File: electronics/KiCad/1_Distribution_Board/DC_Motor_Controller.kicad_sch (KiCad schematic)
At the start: 5 parts, among them J8 Conn_01x02, J9 Conn_01x02

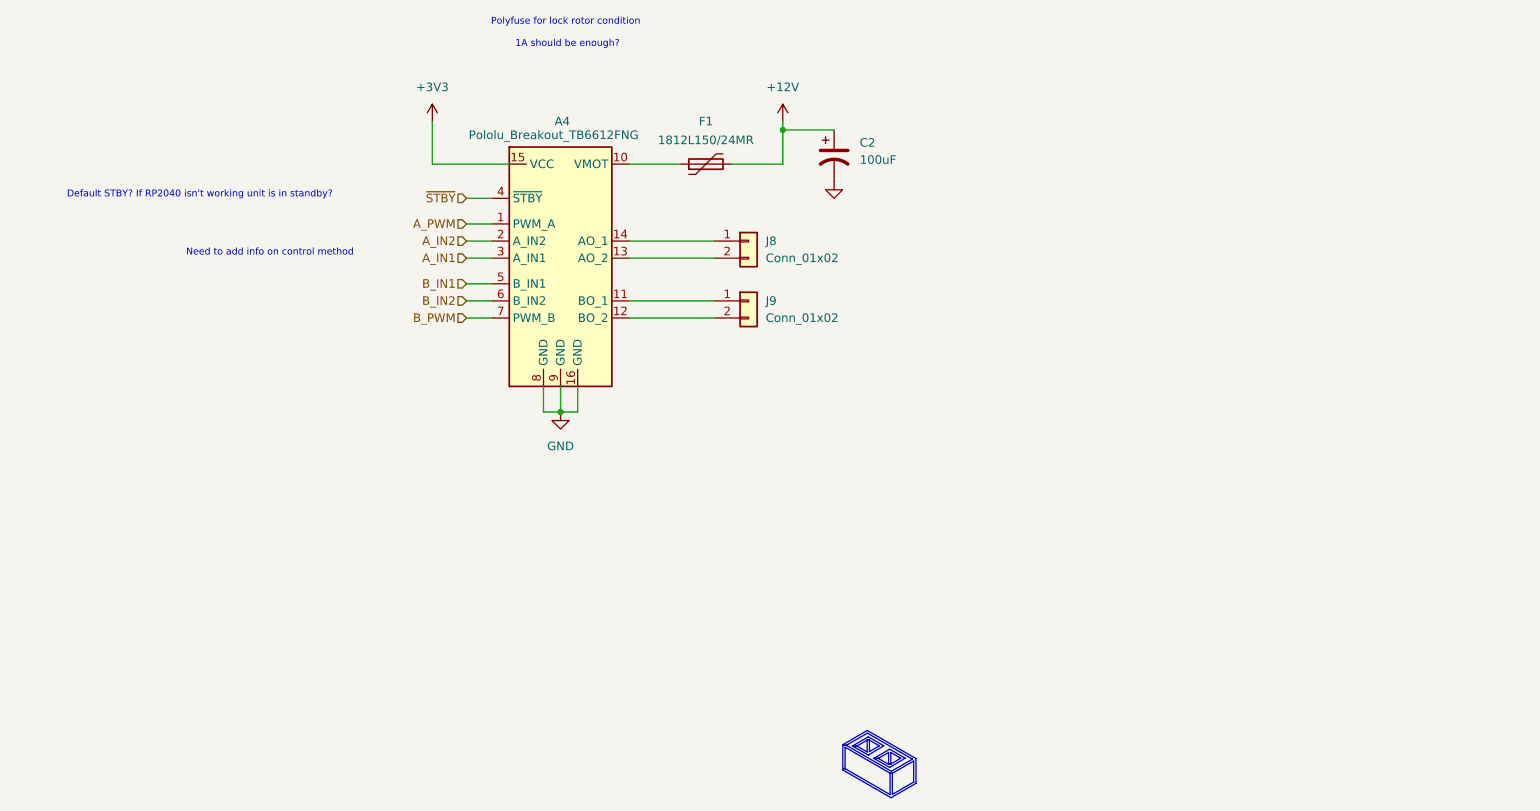
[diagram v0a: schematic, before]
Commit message: Updated Schematic naming, PCB work
Updated Schematic naming for sub-sheets to get rid of untitled and adapter board ones. ADD - 815 sub-sheet for cleaner printable schematic.

PCB:

Started moving modules to socket headers for easy of prototyping.
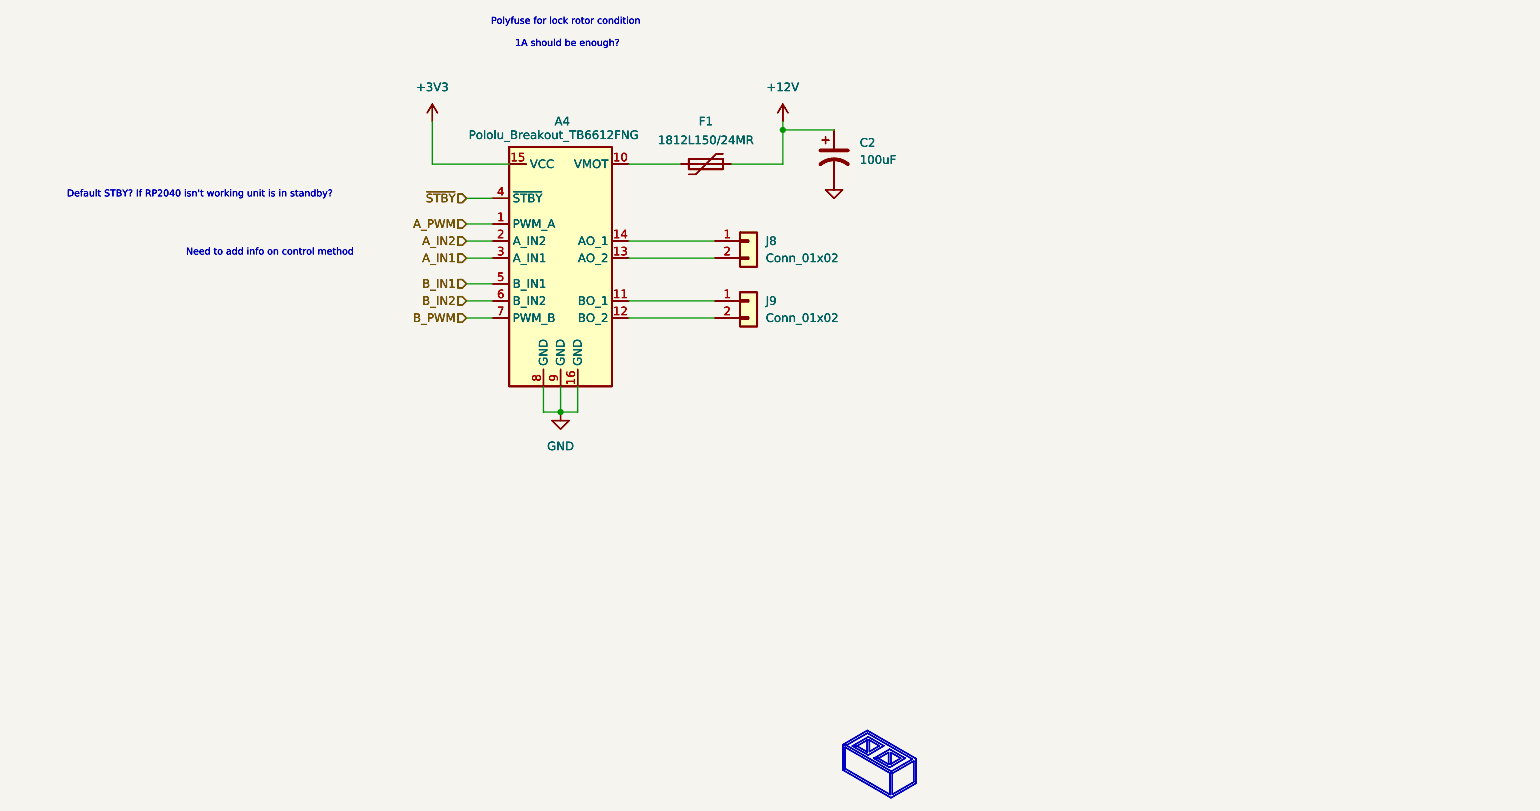
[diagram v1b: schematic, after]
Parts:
- added A4: Pololu_Breakout_TB6612FNG, Module:Pololu_Breakout-16_15.2x20.3mm, symbol JAW:Pololu_Breakout_TB6612FNG
- added C2: 100uF, Capacitor_THT:CP_Radial_D8.0mm_P2.50mm, symbol Device:C_Polarized_US
- added F1: 1812L150/24MR, Fuse:Fuse_1812_4532Metric_Pad1.30x3.40mm_HandSolder, symbol Device:Polyfuse
- added J8, J9: Conn_01x02, Connector_PinHeader_2.54mm:PinHeader_1x02_P2.54mm_Vertical, symbol Connector_Generic:Conn_01x02
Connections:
- net +12V: now also C2.1, F1.2
- net +3V3: now also A4.15 (VCC)
- net A_IN1: now also A4.3 (A_IN1)
- net A_IN2: now also A4.2 (A_IN2)
- net A_PWM: now also A4.1 (PWM_A)
- net B_IN1: now also A4.5 (B_IN1)
- net B_IN2: now also A4.6 (B_IN2)
- net B_PWM: now also A4.7 (PWM_B)
- net GND: now also A4.16 (GND), A4.8 (GND), A4.9 (GND), C2.2
- net ~{STBY}: now also A4.4 (~{STBY})
- net at A4.14 (AO_1), J8.1 (Pin_1): now also A4.14 (AO_1), J8.1 (Pin_1)
- net at A4.13 (AO_2), J8.2 (Pin_2): now also A4.13 (AO_2), J8.2 (Pin_2)
- net at A4.10 (VMOT), F1.1: now also A4.10 (VMOT), F1.1
- net at A4.11 (BO_1), J9.1 (Pin_1): now also A4.11 (BO_1), J9.1 (Pin_1)
- net at A4.12 (BO_2), J9.2 (Pin_2): now also A4.12 (BO_2), J9.2 (Pin_2)

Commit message: PCB updates
Added stepper module headers and working on silk for ease of debug.
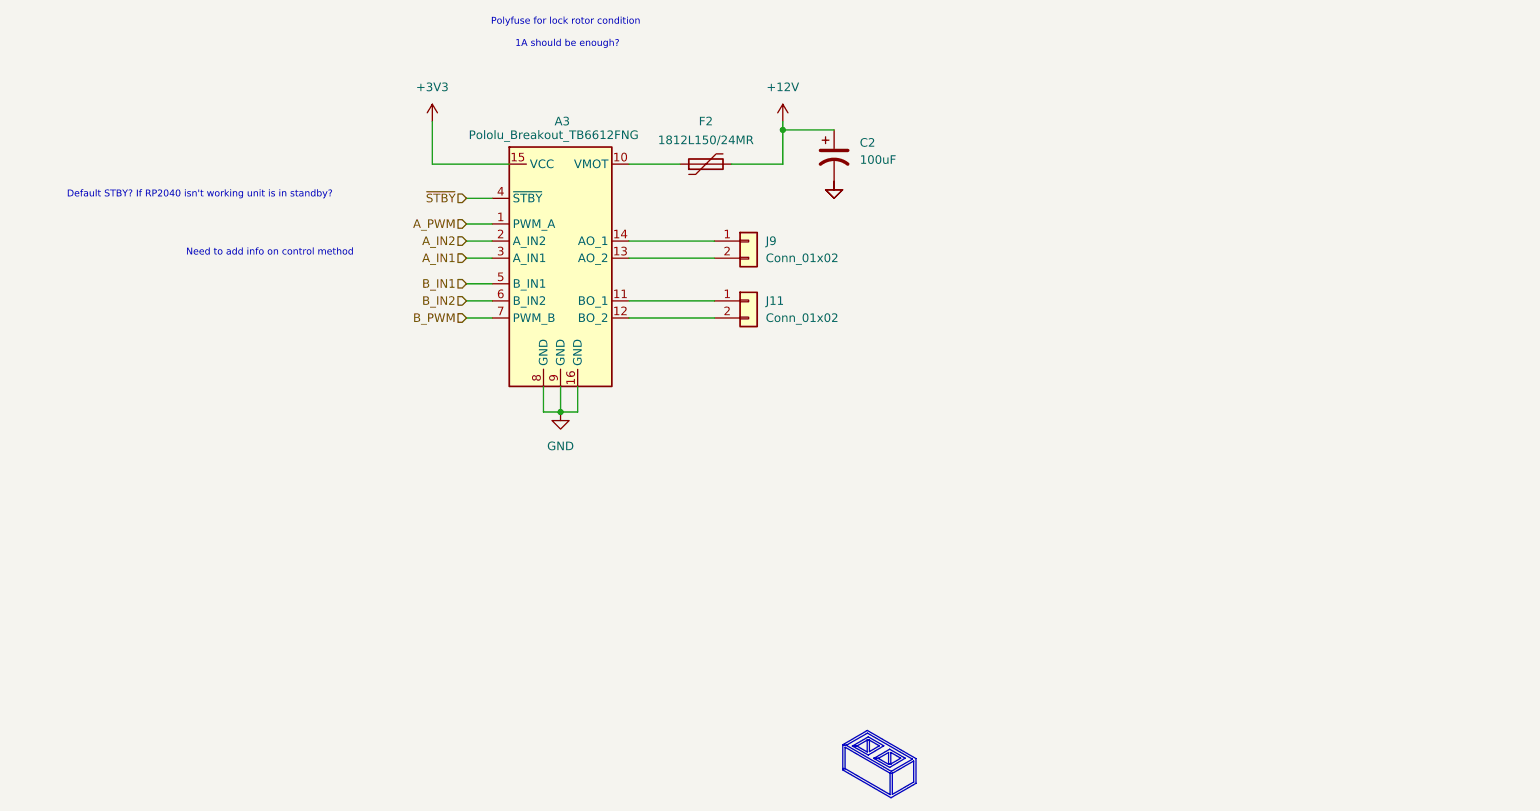
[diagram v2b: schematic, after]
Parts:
- removed A4: Pololu_Breakout_TB6612FNG, Module:Pololu_Breakout-16_15.2x20.3mm, symbol JAW:Pololu_Breakout_TB6612FNG
- removed C2: 100uF, Capacitor_THT:CP_Radial_D8.0mm_P2.50mm, symbol Device:C_Polarized_US
- removed F1: 1812L150/24MR, Fuse:Fuse_1812_4532Metric_Pad1.30x3.40mm_HandSolder, symbol Device:Polyfuse
- removed J8, J9: Conn_01x02, Connector_PinHeader_2.54mm:PinHeader_1x02_P2.54mm_Vertical, symbol Connector_Generic:Conn_01x02
- renumbered A4 to A3, F1 to F2, J9 to J11, J8 to J9

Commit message: Updated PCB/SCH
Updated stepper schematics and motor schematics for clarity. Updated motor module to use headers. Updated stepper driver top be the BIGTREETECH V1.3. Cleaned up layout locations a bit.
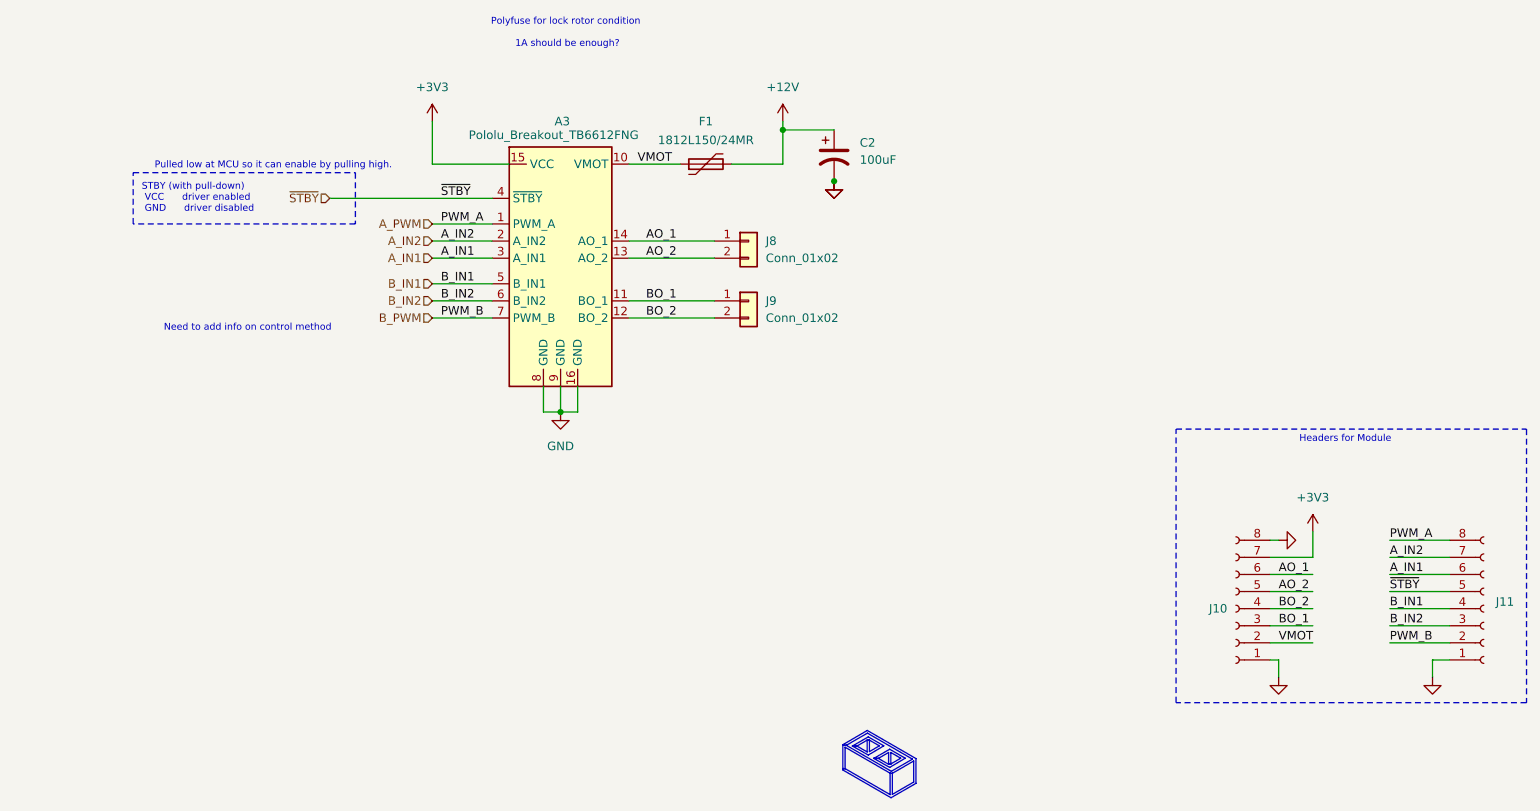
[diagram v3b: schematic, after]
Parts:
- added J10, J11: Conn_01x08_Socket, Connector_PinSocket_2.54mm:PinSocket_1x08_P2.54mm_Vertical, symbol Connector:Conn_01x08_Socket
- A3: now left out of the parts list
- renumbered F2 to F1, J9 to J8, J11 to J9
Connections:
- net +3V3: now also J10.7 (Pin_7)
- net A_IN1: now also J11.6 (Pin_6)
- net A_IN2: now also J11.7 (Pin_7)
- net A_PWM: now also J11.8 (Pin_8)
- net B_IN1: now also J11.4 (Pin_4)
- net B_IN2: now also J11.3 (Pin_3)
- net B_PWM: now also J11.2 (Pin_2)
- net GND: now also J10.1 (Pin_1), J10.8 (Pin_8), J11.1 (Pin_1)
- net ~{STBY}: now also J11.5 (Pin_5)
- net VMOT: now reaches A3.10 (VMOT), F1.1
- net VMOT: now also J10.2 (Pin_2)
- net BO_1: now reaches A3.11 (BO_1), J9.1 (Pin_1)
- net BO_1: now also J10.3 (Pin_3)
- net BO_2: now reaches A3.12 (BO_2), J9.2 (Pin_2)
- net BO_2: now also J10.4 (Pin_4)
- net AO_2: now reaches A3.13 (AO_2), J8.2 (Pin_2)
- net AO_2: now also J10.5 (Pin_5)
- net AO_1: now reaches A3.14 (AO_1), J8.1 (Pin_1)
- net AO_1: now also J10.6 (Pin_6)
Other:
- note added: "Headers for Module"
- note added: "Pulled low at MCU so it can enable by pulling high."
- note added: "STBY (with pull-down) VCC driver enabled GND driver disabled"
- note removed: "Default STBY? If RP2040 isn't working unit is in standby?"

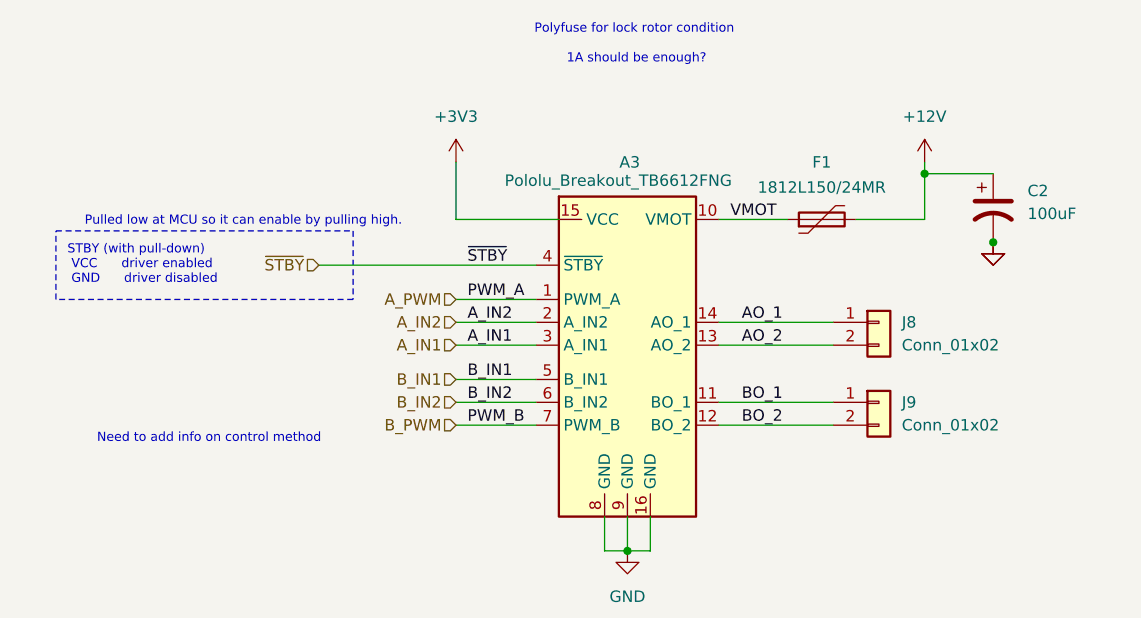
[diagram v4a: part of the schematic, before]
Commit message: SCH Cleanup for review
Cleaned up Processor page and cleaned up all other pages with notes for clarity
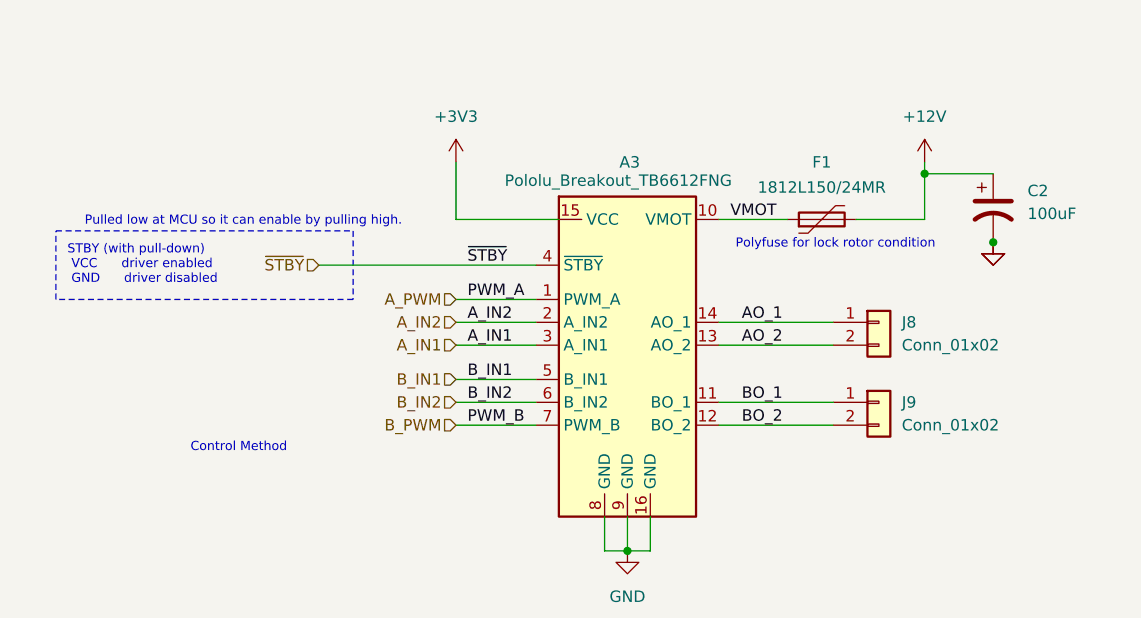
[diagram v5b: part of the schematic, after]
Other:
- note added: "Control Method"
- note removed: "1A should be enough?"
- note removed: "Need to add info on control method"
